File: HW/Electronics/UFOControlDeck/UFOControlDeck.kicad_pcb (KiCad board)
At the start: 4 copper layers, 46 x 46 mm, 104 parts, among them J1 Conn_01x02_Male, J10 Conn_01x02_Male, J13 Conn_02x08_Odd_Even, J2 Conn_02x04_Odd_Even, U1 TPSM84209RKHT, U2 LM555xM, U3 ICE40HX8K-BG121, U4 ASDMB-xxxMHz, U5 SN74LV1T34DBV, U6 MT25QL128ABA, U7 TPSM84209RKHT, U8 TPSM84209RKHT

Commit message: Added control deck Interactive BoM
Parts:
- C1, C2, C3, C4, C5, C6: value C -> 10u
- C10: value C -> 100p
- C11, C12: value C -> 10n
- C13: value C -> 50n
- C15, C16, C17, C18, C19, C20, C21, C22, C23, C24, C25, C26, C27, C28, C29, C30, C31, C32, C33, C34, C35, C36, C37, C38, C42, C43, C44, C45: value C -> 100n
- C39, C40, C41, C7, C8, C9: value C -> 47u
- R1, R10, R11, R12, R13, R25, R26, R27, R28, R29, R3, R30, R4, R5: value R -> 10k
- R16, R17, R18, R19, R20, R21, R22, R23, R24: value R -> 1k
- R2: value R -> 2.21k
- R31: value R -> 2k2
- R6: value R -> 1.37k
- R7, R8: value R -> 100R

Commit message: Starting FPGA part switch to LCMXO3D-4300ZC-3SG72I
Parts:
- removed C41: 47u, Capacitor_SMD:C_0603_1608Metric_Pad1.08x0.95mm_HandSolder
- removed U1, U7, U8: TPSM84209RKHT, TPSM84209:TPSM84209RKHT
- added C49: 50n, Capacitor_SMD:C_0603_1608Metric_Pad1.08x0.95mm_HandSolder, F.Cu at (139.6, 105.5)
- added D2: D_Schottky, Diode_SMD:D_0603_1608Metric_Pad1.05x0.95mm_HandSolder, F.Cu at (136.2, 101.9)
- added H1: MountingHole_Pad, MountingHole:MountingHole_4.3mm_M4_DIN965_Pad, F.Cu at (125.2, 101.8)
- added H2: MountingHole_Pad, MountingHole:MountingHole_4.3mm_M4_DIN965_Pad, F.Cu at (125.2, 128.7)
- added H3: MountingHole_Pad, MountingHole:MountingHole_4.3mm_M4_DIN965_Pad, F.Cu at (152.1, 101.8)
- added H4: MountingHole_Pad, MountingHole:MountingHole_4.3mm_M4_DIN965_Pad, F.Cu at (152.1, 128.7)
- added J3: Conn_01x02_Male, Connector_PinHeader_1.27mm:PinHeader_1x02_P1.27mm_Vertical, F.Cu at (179.3, 114.3)
- added R32: 10k, Resistor_SMD:R_0603_1608Metric_Pad0.98x0.95mm_HandSolder, F.Cu at (140.6, 103.0)
- added R33: 200K, Resistor_SMD:R_0603_1608Metric_Pad0.98x0.95mm_HandSolder, F.Cu at (106.2, 127.5)
- added R34: 142K, Resistor_SMD:R_0603_1608Metric_Pad0.98x0.95mm_HandSolder, F.Cu at (97.5, 135.0)
- added R35: 14.3K, Resistor_SMD:R_0603_1608Metric_Pad0.98x0.95mm_HandSolder, F.Cu at (101.9, 132.5)
- added RV1: R_POT, Potentiometer_SMD:Potentiometer_Bourns_3214W_Vertical, F.Cu at (131.8, 103.6)
- added U9: LTC6752xUD-3, Package_DFN_QFN:QFN-12-1EP_3x3mm_P0.5mm_EP1.65x1.65mm, F.Cu at (140.4, 99.2)
- C1, C5: value 10u -> 1u; moved to F.Cu
- C12: value 10n -> C
- C2, C3, C6: moved to F.Cu
- C39, C40, C8, C9: value 47u -> 10u; moved to F.Cu
- C4: value 10u -> 47u; moved to F.Cu
- C7: value 47u -> 1u; moved to F.Cu
- J2: value Conn_02x04_Odd_Even -> Conn_02x08_Counter_Clockwise; footprint Connector_PinHeader_1.27mm:PinHeader_2x04_P1.27mm_Vertical_SMD -> Connector_PinSocket_1.27mm:PinSocket_2x08_P1.27mm_Vertical_SMD
- R1: value 10k -> 200K
- R2: value 2.21k -> 35.65K
- R4, R5: value 10k -> 100k
- R6: value 1.37k -> 75K
- R9: value R -> 10k
- U2: value LM555xM -> SN74LV1T34DBV; footprint Package_SO:SOIC-8_3.9x4.9mm_P1.27mm -> Package_TO_SOT_SMD:SOT-23-5
- U6: value MT25QL128ABA -> W25Q128JVS; footprint Package_DFN_QFN:DFN-8-1EP_6x5mm_P1.27mm_EP2x2mm -> Package_SO:SOIC-8_5.23x5.23mm_P1.27mm
- moved C5 42.0 mm to (93.2, 132.5)
- moved C2 40.0 mm to (93.2, 127.5)
- moved C1 39.5 mm to (84.7, 115.9)
- moved C40 39.2 mm to (93.2, 135.0)
- moved J10 37.0 mm to (181.7, 114.3)
- moved R6 35.4 mm to (89.0, 119.9), turned to 0 degrees
- moved C6 34.6 mm to (84.7, 117.4), turned to 0 degrees
- moved R1 34.5 mm to (84.7, 119.9), turned to 0 degrees
- moved R3 34.4 mm to (97.5, 132.5), turned to 0 degrees
- moved C8 33.7 mm to (97.5, 130.0)
- moved R2 31.8 mm to (89.0, 117.4), turned to 0 degrees
- moved C9 30.5 mm to (89.0, 114.9), turned to 0 degrees
- moved R5 29.3 mm to (93.4, 114.9), turned to 0 degrees
- moved C4 28.5 mm to (97.5, 127.5)
- moved R4 28.4 mm to (101.9, 130.0), turned to 0 degrees
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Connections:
- C1 pad 1: +VSW -> +5V
- C12 pad 1: Net-(C12-Pad1) -> GND
- C12 pad 2: GND -> +3V3
- C13 pad 2: Net-(C13-Pad2) -> /Q
- C2 pad 1: +VSW -> +5V
- C3 pad 1: +VSW -> Net-(C3-Pad1)
- C39 pad 1: +3V3 -> +5V
- C4 pad 1: +VSW -> +5V
- C4 pad 2: GND -> Net-(C4-Pad2)
- C40 pad 1: +1V2 -> +5V
- C48 pad 1: +5V -> +3V3
- C5 pad 1: +VSW -> +1V2
- C8 pad 1: +1V2 -> +5V
- D1 pad 2: Net-(D1-Pad2) -> CDONE
- D4 pad 1: Net-(D4-Pad1) -> +3V3
- J10 pad 1: TRIGGER -> ~TRIGGER
- J2 pad 2: SDI -> GND
- J2 pad 3: GND -> Net-(J2-Pad3)
- J2 pad 4: FLASH_WP -> SCK
- J2 pad 6: HOLD_RST -> Net-(J2-Pad6)
- J2 pad 7: SCK -> Net-(J2-Pad7)
- J2 pad 8: SDO -> Net-(J2-Pad8)
- R10 pad 2: Net-(R10-Pad2) -> CRESET
- R11 pad 1: Net-(D4-Pad1) -> +3V3
- R12 pad 2: Net-(C13-Pad2) -> /Q
- R13 pad 1: +5V -> Net-(C10-Pad1)
- R13 pad 2: Net-(C12-Pad1) -> GND
- R25 pad 1: SS_FLASH -> SCK
- R27 pad 1: SDI -> SS_FLASH
- R28 pad 1: SCK -> SDO
- R29 pad 1: SDO -> SDI
- R3 pad 1: +1V2 -> +5V
- R3 pad 2: Net-(R3-Pad2) -> Net-(C3-Pad1)
- R31 pad 2: Net-(R31-Pad2) -> CDONE
- R4 pad 1: Net-(R3-Pad2) -> Net-(R4-Pad1)
- R4 pad 2: GND -> Net-(R4-Pad2)
- R5 pad 1: +5V -> +VSW
- R6 pad 1: Net-(R5-Pad2) -> +5V
- R6 pad 2: GND -> Net-(C4-Pad2)
- R9 pad 1: Net-(R31-Pad2) -> Net-(J2-Pad11)
- R9 pad 2: Net-(D1-Pad2) -> CRESET
- U2 pad 1: GND -> Net-(U2-Pad1)
- U2 pad 2: Net-(C10-Pad1) -> /Q
- U2 pad 3: Net-(C13-Pad2) -> GND
- U2 pad 4: +5V -> TRIGGER
- U2 pad 5: Net-(C11-Pad1) -> +3V3
- U3 pad K8: Net-(R31-Pad2) -> CDONE
- U3 pad L2: Net-(U3-PadL2) -> ~TRIGGER
- U3 pad L9: Net-(R10-Pad2) -> CRESET
- U5 pad 2: Net-(C13-Pad2) -> /~Q
- U5 pad 4: TRIGGER -> ~TRIGGER
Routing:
- net SCK: track 48.2 -> 4.58 mm
- net SDO: track 36.8 -> 3.09 mm
- net SDI: track 33.3 -> 0.00 mm
- net SS_FLASH: track 29.8 -> 0.00 mm, vias 2 -> 0
- net PULSE1: track 28.9 -> 0.48 mm, vias 1 -> 0
- net PULSE0: track 28.3 -> 0.38 mm, vias 1 -> 0
- net PULSE3: track 27.1 -> 0.00 mm, vias 1 -> 0
- net PULSE2: track 27.0 -> 0.77 mm, vias 1 -> 0
- net PULSE4: track 25.8 -> 0.00 mm, vias 1 -> 0
- net PULSE5: track 25.3 -> 0.00 mm, vias 1 -> 0
- net PULSE6: track 23.9 -> 0.00 mm, vias 1 -> 0
- net PULSE7: track 23.2 -> 0.58 mm, vias 1 -> 0
- net +3V3: track 56.4 -> 34.1 mm, vias 35 -> 23
- net GND: track 33.3 -> 13.9 mm, vias 113 -> 18
- net Net-(R31-Pad2): track 17.5 -> 0.00 mm, vias 3 -> 0
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- removed copper zone on B.Cu, net +5V
- removed copper zone on F.Cu, net +5V
- removed copper zone on In2.Cu, net +5V
- removed copper zone on B.Cu, net +VSW
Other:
- outline, holes or cut-outs redrawn
- rule trace_min: 0.13 -> 0.09

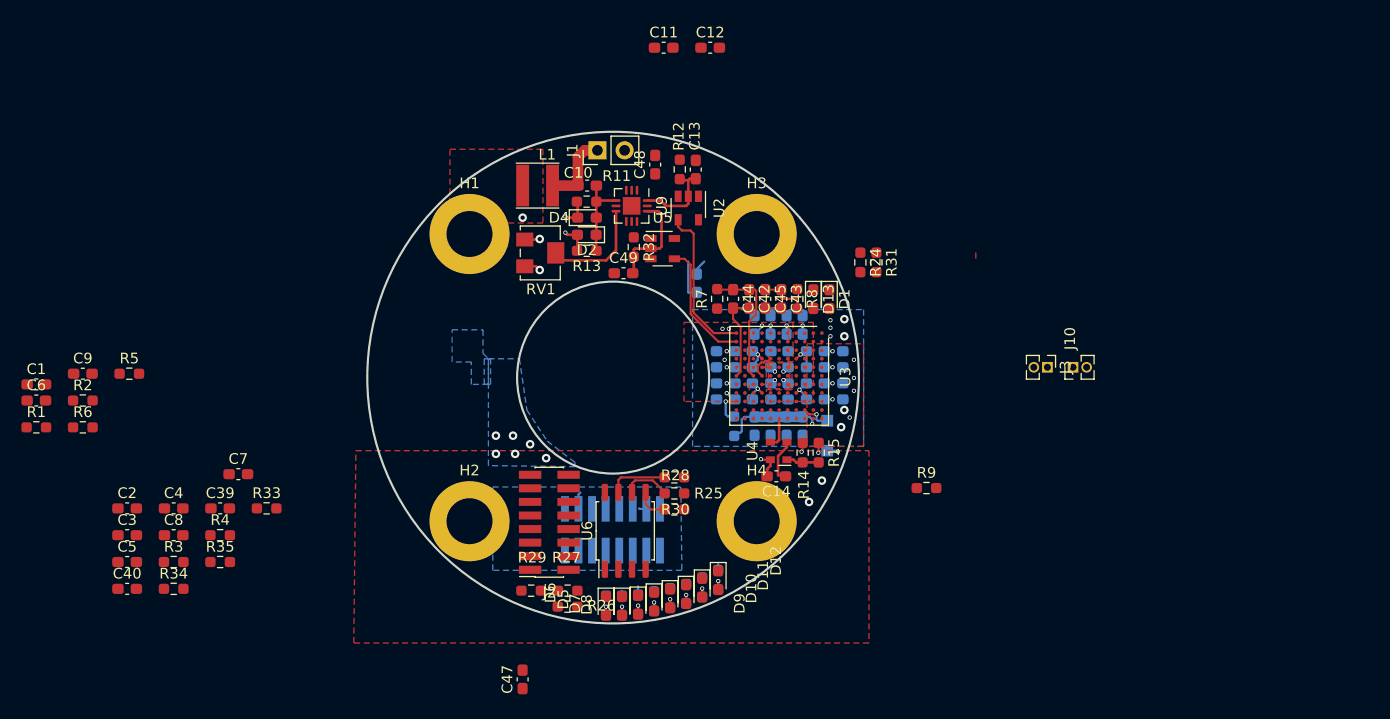
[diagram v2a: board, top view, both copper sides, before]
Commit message: pcb and schematic changes for machxo3d
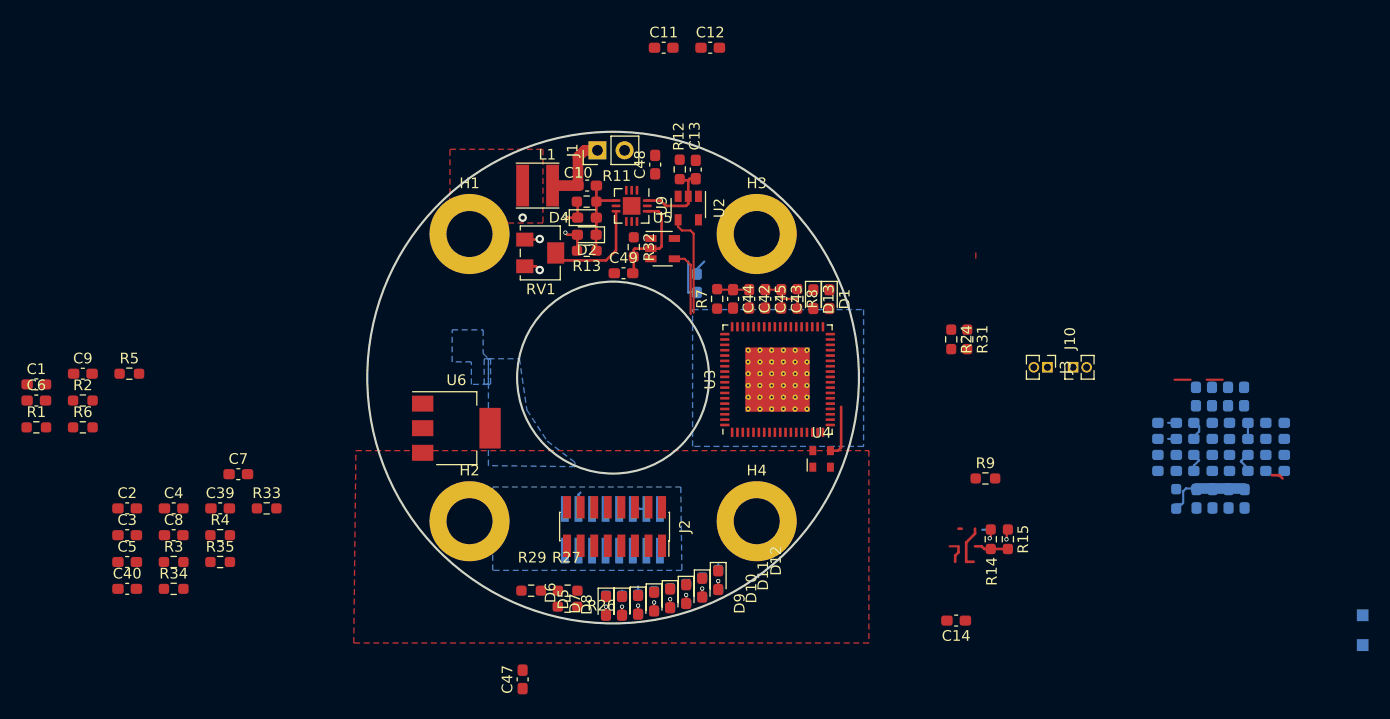
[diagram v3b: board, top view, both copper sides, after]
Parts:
- removed R25, R28, R30: 10k, Resistor_SMD:R_0603_1608Metric_Pad0.98x0.95mm_HandSolder
- U3: value ICE40HX8K-BG121 -> LCMXO3D-4300ZC-3SG72I; footprint Package_BGA:BGA-121_9.0x9.0mm_Layout11x11_P0.8mm_Ball0.4mm_Pad0.35mm_NSMD -> Package_DFN_QFN:QFN-72-1EP_10x10mm_P0.5mm_EP6x6mm_ThermalVias
- U6: value W25Q128JVS -> NCP1117-3.3_SOT223; footprint Package_SO:SOIC-8_5.23x5.23mm_P1.27mm -> Package_TO_SOT_SMD:SOT-223-3_TabPin2
- moved D14 53.3 mm to (208.8, 138.9)
- moved C18 41.9 mm to (193.2, 126.6)
- moved C19 41.9 mm to (194.8, 126.6)
- moved C20 41.9 mm to (196.2, 126.6)
- moved C29 41.9 mm to (197.8, 126.6)
- moved R10 41.9 mm to (191.3, 126.6)
- moved C21 41.8 mm to (190.5, 119.5)
- moved C22 41.8 mm to (190.5, 121.0)
- moved C23 41.8 mm to (190.5, 122.5)
- moved C32 41.8 mm to (193.9, 119.5)
- moved C34 41.8 mm to (193.9, 124.0)
- moved C35 41.8 mm to (193.9, 122.5)
- moved C36 41.8 mm to (190.5, 124.0)
- moved C38 41.8 mm to (193.9, 121.0)
- moved C15 41.8 mm to (200.6, 121.0)
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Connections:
- U6 pad 1: SS_FLASH -> GND
- U6 pad 2: SDI -> +3V3
- U6 pad 3: FLASH_WP -> +5V
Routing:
- net +3V3: track 34.1 -> 21.4 mm, vias 23 -> 3
- net Net-(C42-Pad1): track 12.1 -> 3.02 mm
- net Net-(C42-Pad2): track 8.31 -> 1.51 mm
- net HOLD_RST: track 5.58 -> 0.00 mm
- net ~TRIGGER: track 11.7 -> 6.35 mm
- net TRIGGER: track 14.6 -> 9.77 mm
- net SCK: track 4.58 -> 0.00 mm
- net CLK: track 3.20 -> 6.35 mm
- net CRESET: track 3.12 -> 0.00 mm, vias 1 -> 0
- net SDO: track 3.09 -> 0.00 mm
- net +1V2: track 9.97 -> 7.16 mm, vias 10 -> 0
- net Net-(D14-Pad1): track 2.81 -> 0.00 mm, vias 1 -> 0
- net GND: track 13.9 -> 13.1 mm, vias 18 -> 3
- removed copper zone on F.Cu, net +3V3

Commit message: main changes made to swap fpga, comparator and power supplies
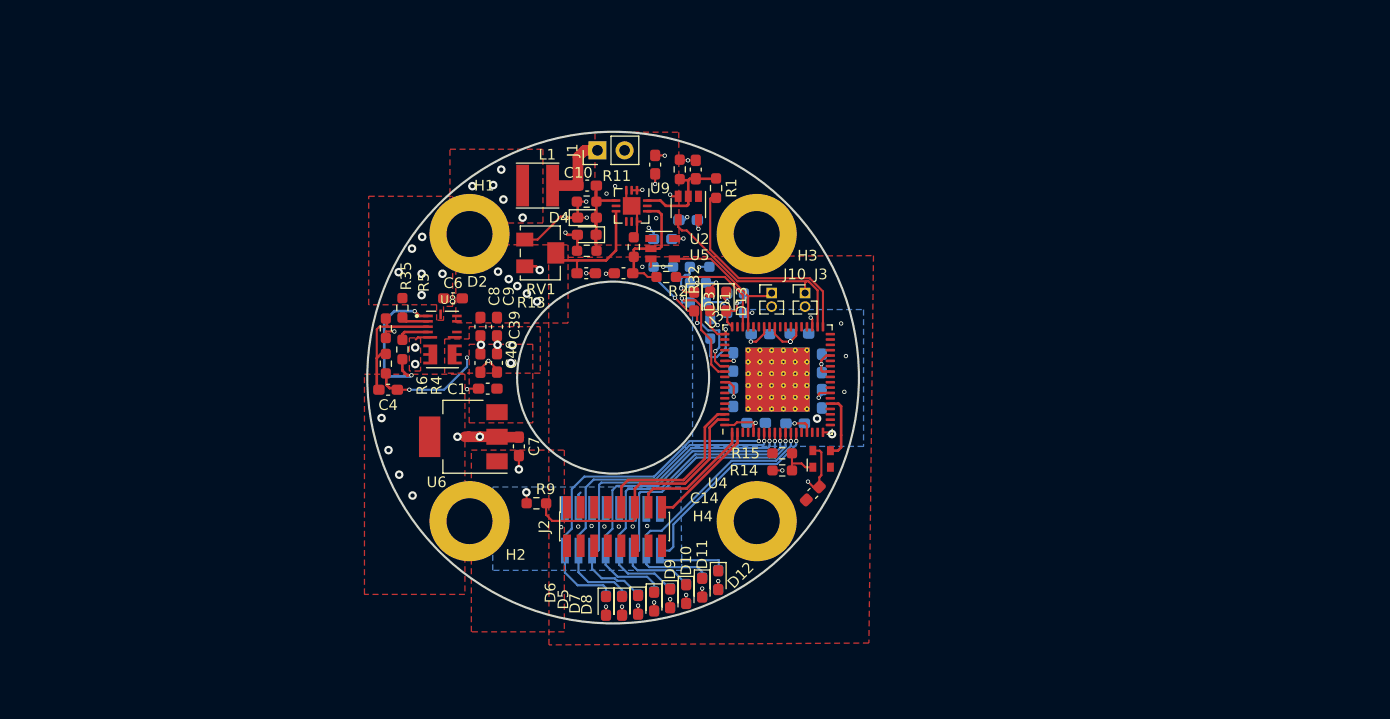
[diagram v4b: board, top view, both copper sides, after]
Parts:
- removed C15, C16, C17, C18, C19, C20, C21, C22, C23, C24, C25, C26, C27, C28, C29, C36, C42, C43, C44, C45: 100n, Capacitor_SMD:C_0603_1608Metric_Pad1.08x0.95mm_HandSolder
- removed C2, C3: 10u, Capacitor_SMD:C_0603_1608Metric_Pad1.08x0.95mm_HandSolder
- removed C47: C, Capacitor_SMD:C_0603_1608Metric_Pad1.08x0.95mm_HandSolder
- removed C5: 1u, Capacitor_SMD:C_0603_1608Metric_Pad1.08x0.95mm_HandSolder
- removed D14: D_Schottky, Diode_SMD:D_SOD-123F
- removed R27, R29: 10k, Resistor_SMD:R_0603_1608Metric_Pad0.98x0.95mm_HandSolder
- removed R31: 2k2, Resistor_SMD:R_0603_1608Metric_Pad0.98x0.95mm_HandSolder
- removed R33: 200K, Resistor_SMD:R_0603_1608Metric_Pad0.98x0.95mm_HandSolder
- removed R34: 142K, Resistor_SMD:R_0603_1608Metric_Pad0.98x0.95mm_HandSolder
- added D3: LED, LED_SMD:LED_0603_1608Metric_Pad1.05x0.95mm_HandSolder, F.Cu at (146.2, 108.2)
- added R25: 1k, Resistor_SMD:R_0603_1608Metric_Pad0.98x0.95mm_HandSolder, B.Cu at (145.8, 107.3)
- added U8: RPX-1.5-tony_bits, Recom:CONV_RPX-1.5-R, F.Cu at (122.7, 111.7)
- C12, R24, R26: moved to B.Cu
- C4: value 47u -> 22p
- J2: value Conn_02x08_Counter_Clockwise -> Conn_02x08_Odd_Even
- R1: value 200K -> 0r
- R2: value 35.65K -> 0r
- R3: value 10k -> 1k; moved to B.Cu
- R7: value 100R -> 1k; moved to B.Cu
- R8: value 100R -> 10k; moved to B.Cu
- R9: value 10k -> 1k
- moved R1 67.4 mm to (148.3, 97.5), turned to 270 degrees
- moved R3 55.8 mm to (147.3, 107.3), turned to 270 degrees
- moved R2 55.8 mm to (143.6, 105.8), turned to 180 degrees
- moved R10 46.4 mm to (147.8, 110.7)
- moved C37 46.2 mm to (152.4, 111.2), turned to 0 degrees
- moved C35 44.8 mm to (149.9, 113.8), turned to 270 degrees
- moved C34 44.5 mm to (149.9, 117.1), turned to 270 degrees
- moved C1 42.2 mm to (126.9, 116.3), turned to 180 degrees
- moved R9 42.1 mm to (131.5, 127.0), turned to 180 degrees
- moved C32 41.8 mm to (152.1, 119.5)
- moved C31 41.7 mm to (155.7, 119.5), turned to 0 degrees
- moved C40 40.5 mm to (127.8, 113.9), turned to 270 degrees
- moved C6 40.1 mm to (123.7, 107.8)
- moved C33 39.6 mm to (158.2, 113.9), turned to 90 degrees
- moved C30 39.1 mm to (158.2, 117.2), turned to 270 degrees
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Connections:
- net HOLD_RST renamed Net-(J2-Pad14)
- C30 pad 1: +1V2 -> +3V3
- C31 pad 1: +1V2 -> +3V3
- C32 pad 1: +1V2 -> +3V3
- C33 pad 1: +1V2 -> +3V3
- C34 pad 1: +1V2 -> +3V3
- C35 pad 1: +1V2 -> +3V3
- C37 pad 1: +1V2 -> +3V3
- C38 pad 1: +1V2 -> +3V3
- D1 pad 1: GND -> Net-(D1-Pad1)
- D1 pad 2: CDONE -> Net-(D1-Pad2)
- D13 pad 1: GND -> Net-(D13-Pad1)
- J2 pad 1: SS_FLASH -> Net-(J2-Pad1)
- J2 pad 11: Net-(J2-Pad11) -> TCK
- J2 pad 12: CDONE -> Net-(J2-Pad12)
- J2 pad 13: SDO -> TDI
- J2 pad 15: FLASH_WP -> TDO
- J2 pad 16: SDI -> Net-(J2-Pad16)
- J2 pad 2: GND -> Net-(J2-Pad2)
- J2 pad 4: SCK -> Net-(J2-Pad4)
- J2 pad 7: Net-(J2-Pad7) -> GND
- J2 pad 9: Net-(J2-Pad9) -> TMS
- R1 pad 1: +3V3 -> /Q
- R1 pad 2: Net-(R1-Pad2) -> COMP
- R10 pad 1: +3V3 -> Net-(D1-Pad2)
- R10 pad 2: CRESET -> +3V3
- R2 pad 1: Net-(R1-Pad2) -> ~COMP
- R2 pad 2: GND -> /~Q
- R24 pad 1: Net-(R24-Pad1) -> Net-(D13-Pad1)
- R24 pad 2: Net-(D13-Pad2) -> GND
- R26 pad 1: FLASH_WP -> Net-(D3-Pad2)
- R3 pad 1: +5V -> Net-(D1-Pad1)
- R3 pad 2: Net-(C3-Pad1) -> GND
- R7 pad 1: +1V2 -> Net-(D3-Pad1)
- R7 pad 2: Net-(C42-Pad1) -> GND
- R8 pad 1: +1V2 -> Net-(D13-Pad2)
- R8 pad 2: Net-(C43-Pad1) -> +3V3
- R9 pad 1: Net-(J2-Pad11) -> TCK
- R9 pad 2: CRESET -> GND
- U3 pad 1: SDI -> TDI
- U3 pad 10: Net-(U3-Pad10) -> PULSE4
- U3 pad 11: Net-(U3-Pad11) -> PULSE5
- U3 pad 12: Net-(U3-Pad12) -> PULSE6
- U3 pad 13: Net-(U3-Pad13) -> PULSE7
- U3 pad 2: SDO -> TDO
- U3 pad 37: Net-(U3-Pad37) -> COMP
- U3 pad 38: Net-(U3-Pad38) -> TRIGGER
- U3 pad 51: Net-(U3-Pad51) -> ~TRIGGER
- U3 pad 52: Net-(U3-Pad52) -> ~COMP
- U3 pad 54: Net-(U3-Pad54) -> Net-(D13-Pad2)
- U3 pad 55: Net-(U3-Pad55) -> Net-(D1-Pad2)
- U3 pad 6: Net-(U3-Pad6) -> PULSE0
- U3 pad 61: Net-(U3-Pad61) -> Net-(D3-Pad2)
- U3 pad 7: Net-(U3-Pad7) -> PULSE1
- U3 pad 70: SS_FLASH -> TMS
- U3 pad 71: SCK -> TCK
- U3 pad 73: Net-(U3-Pad73) -> GND
- U3 pad 8: Net-(U3-Pad8) -> PULSE2
- U3 pad 9: Net-(U3-Pad9) -> PULSE3
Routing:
- net +3V3: track 21.4 -> 57.1 mm, vias 3 -> 30
- net PULSE0: track 0.38 -> 33.8 mm, vias 0 -> 1
- net PULSE1: track 0.48 -> 33.5 mm, vias 0 -> 1
- net PULSE2: track 0.77 -> 32.5 mm, vias 0 -> 1
- net PULSE3: track 0.00 -> 31.6 mm, vias 0 -> 1
- net PULSE4: track 0.00 -> 30.4 mm, vias 0 -> 1
- net PULSE5: track 0.00 -> 29.9 mm, vias 0 -> 1
- net PULSE6: track 0.00 -> 27.0 mm, vias 0 -> 1
- net PULSE7: track 0.58 -> 26.4 mm, vias 0 -> 1
- net TCK: track 0.00 -> 25.4 mm
- net COMP: track 0.00 -> 20.8 mm
- net GND: track 13.1 -> 31.7 mm, vias 3 -> 37
- net TMS: track 0.00 -> 16.1 mm
- net Net-(R4-Pad2): track 0.00 -> 14.2 mm, vias 0 -> 2
- net Net-(D3-Pad2): track 0.00 -> 13.8 mm, vias 0 -> 3
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- added copper zone on F.Cu, net +3V3
- added copper zone on F.Cu, net +5V
- added copper zone on In2.Cu, net +5V
- removed copper zone on B.Cu, net +1V2
- removed copper zone on In2.Cu, net +1V2

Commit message: v0.2 design manufactured but requires fixing drill size and traces as not supported by manufacturer
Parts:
- added G***: LOGO, ufoLogo:logo, F.Cu at (122.9, 111.8)
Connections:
- net Net-(D1-Pad2) renamed /INITN
- net Net-(D13-Pad2) renamed /DONE
- net Net-(D3-Pad2) renamed /PROGRAMN
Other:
- rule via_min_drill: 0.2 -> 0.25
- rule via_min_size: 0.25 -> 0.4
- board text added: "UFO Control Deck v0.2"
